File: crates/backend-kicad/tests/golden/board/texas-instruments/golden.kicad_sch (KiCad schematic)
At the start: 1 part, among them U1 U

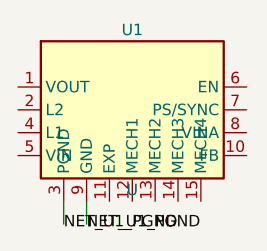
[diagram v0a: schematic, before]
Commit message: Improve recognition of bypass caps
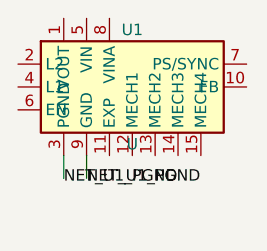
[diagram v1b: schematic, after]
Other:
- moved on the sheet: U1
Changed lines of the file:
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@@
   (symbol
     (lib_id "copperleaf:TPS63031DSKR")
-    (at 40.64 38.1 0)
+    (at 40.64 35.56 0)
     (unit 1)
     (in_bom yes)
@@
           (size 1.27 1.27))))
     (property "Value" "U"
-      (at 40.64 46.99 0)
+      (at 40.64 41.91 0)
       (effects
         (font
           (size 1.27 1.27))))
     (property "Footprint" "TPS63031DSKR"
-      (at 40.64 38.1 0)
+      (at 40.64 35.56 0)
       (hide yes)
       (effects
@@
   (wire
     (pts
-      (xy 33.02 48.26)
-      (xy 33.02 50.8))
+      (xy 33.02 43.18)
+      (xy 33.02 45.72))
     (stroke
       (width 0))
 )
   (label "NET_U1_PGND"
-    (at 33.02 50.8 0)
+    (at 33.02 45.72 0)
     (effects
       (font
@@
   (wire
     (pts
-      (xy 35.56 48.26)
-      (xy 35.56 50.8))
+      (xy 35.56 43.18)
+      (xy 35.56 45.72))
     (stroke
       (width 0))
 )
   (label "NET_U1_PGND"
-    (at 35.56 50.8 0)
+    (at 35.56 45.72 0)
     (effects
       (font
